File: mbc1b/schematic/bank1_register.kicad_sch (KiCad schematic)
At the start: 9 parts

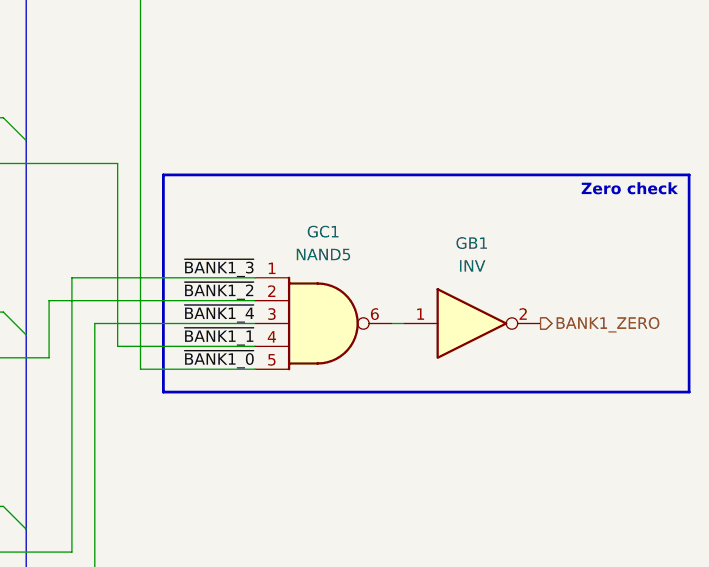
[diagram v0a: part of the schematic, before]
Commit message: Update MBC1B schematic with latest kingfish compatibility
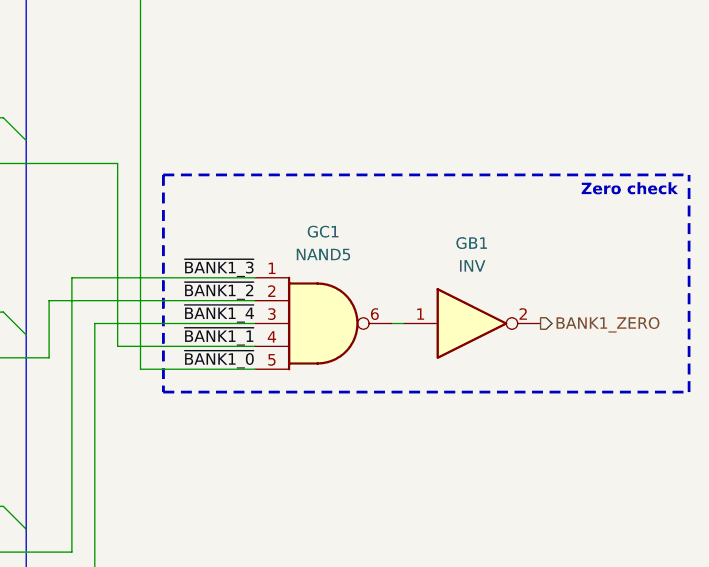
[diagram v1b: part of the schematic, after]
